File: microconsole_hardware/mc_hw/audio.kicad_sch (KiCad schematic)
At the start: 46 parts, among them U20 PCM5102APWR, U21 PAM8302AADCR, U22 PAM8406DR

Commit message: update
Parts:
- added FB2, FB3: FerriteBead_Small, PCM_SparkFun-Capacitor:C_0603_1608Metric, symbol Device:FerriteBead_Small
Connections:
- net 3v3: now also FB3.1
- net 3v3_AUDIO: now also FB3.2
- net AMP_VDD: now also FB2.2
- new net VBUS: FB2.1

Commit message: charging pass
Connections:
- net VBUS renamed VSYS_BAT

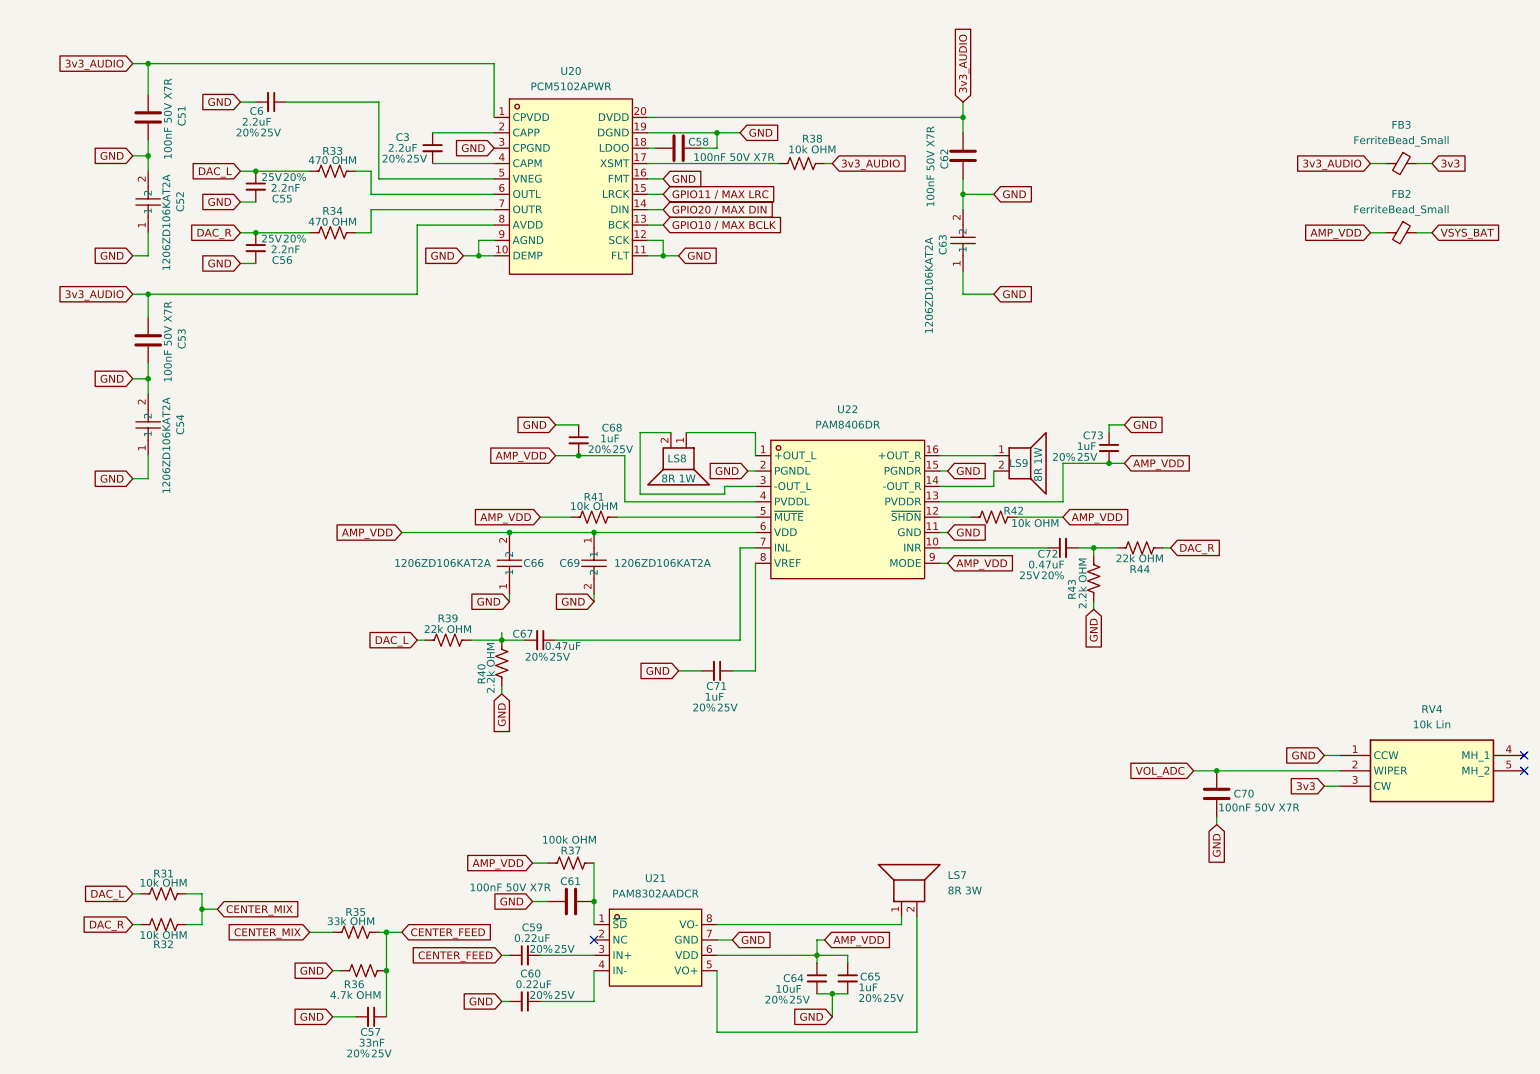
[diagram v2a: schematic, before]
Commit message: recover lost pages
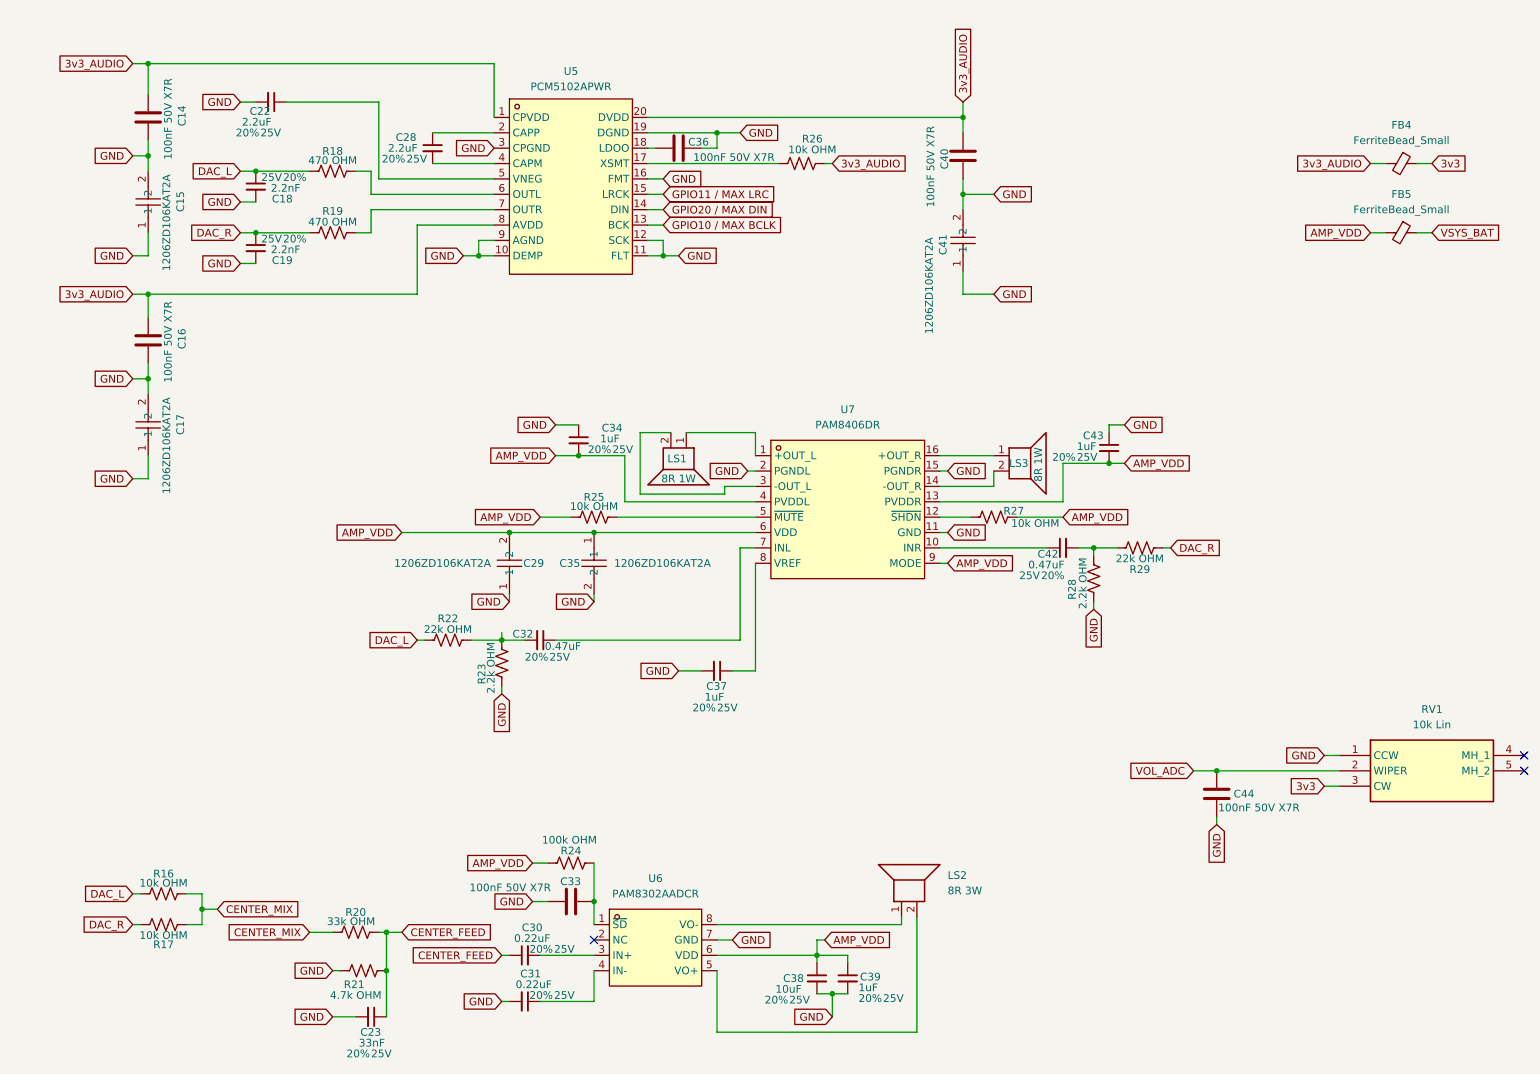
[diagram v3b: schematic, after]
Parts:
- renumbered C51 to C14, C52 to C15, C53 to C16, C54 to C17, C55 to C18, C56 to C19, C6 to C22, C57 to C23, C3 to C28, C66 to C29, C59 to C30, C60 to C31, C67 to C32, C61 to C33, C68 to C34, C69 to C35, C58 to C36, C71 to C37, C64 to C38, C65 to C39, C62 to C40, C63 to C41, C72 to C42, C73 to C43, C70 to C44, FB3 to FB4, FB2 to FB5, LS8 to LS1, LS7 to LS2, LS9 to LS3, R31 to R16, R32 to R17, R33 to R18, R34 to R19, R35 to R20, R36 to R21, R39 to R22, R40 to R23, R37 to R24, R41 to R25, R38 to R26, R42 to R27, R43 to R28, R44 to R29, RV4 to RV1, U20 to U5, U21 to U6, U22 to U7

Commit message: fix a bunch of footprints and routing
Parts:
- FB4, FB5: footprint PCM_SparkFun-Capacitor:C_0603_1608Metric -> Ferrite_THT:LairdTech_28C0236-0JW-10
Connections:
- net 3v3_AUDIO: now also C15.2, C17.2, C41.2
- net GND: no longer C15.2, C17.2, C41.2
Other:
- moved on the sheet: C14, C15, C17, C22, C40, C41

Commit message: fix up
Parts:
- FB4, FB5: footprint Ferrite_THT:LairdTech_28C0236-0JW-10 -> (none)
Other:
- moved on the sheet: LS2

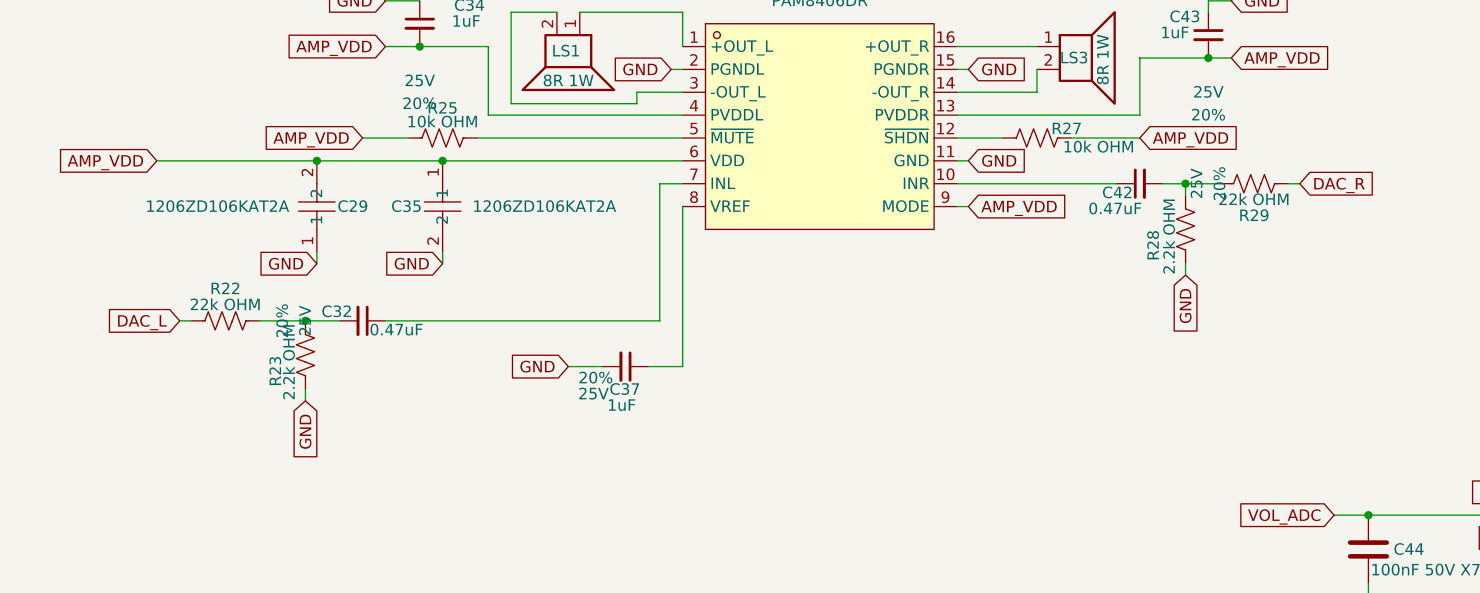
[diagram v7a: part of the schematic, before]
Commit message: fix audio gain, relocated shoulder buttons, round pcb edges
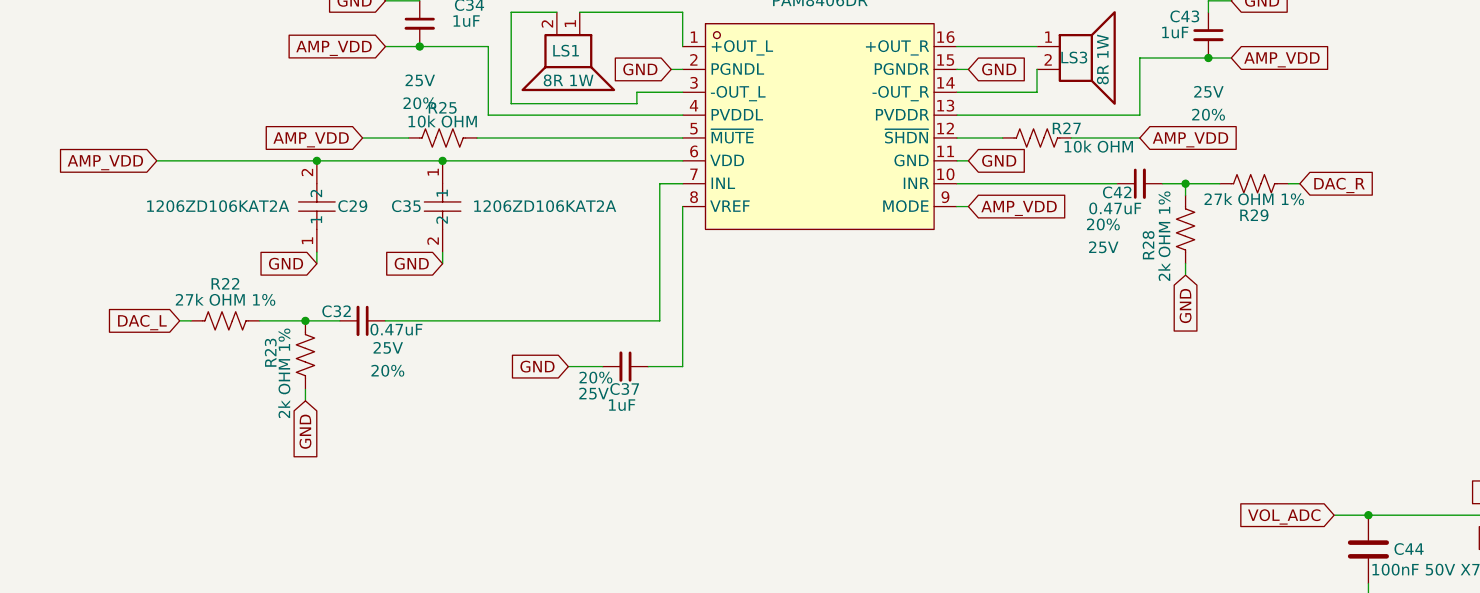
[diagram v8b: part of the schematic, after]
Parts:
- R22, R29: value 22k OHM -> 27k OHM 1%
- R23, R28: value 2.2k OHM -> 2k OHM 1%
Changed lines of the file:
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@@
 		)
 		(property "Voltage" "25V"
-			(at 191.77 107.95 0)
+			(at 181.356 115.062 90)
 			(show_name no)
 			(do_not_autoplace no)
@@
 		)
 		(property "Tolerance" "20%"
-			(at 194.31 107.95 0)
+			(at 181.356 112.522 90)
 			(show_name no)
 			(do_not_autoplace no)
@@
 		(dnp no)
 		(property "Reference" "R28"
-			(at 186.944 114.808 0)
+			(at 186.436 114.808 0)
 			(show_name no)
 			(do_not_autoplace no)
@@
 			)
 		)
-		(property "Value" "2.2k OHM"
-			(at 188.722 113.792 0)
+		(property "Value" "2k OHM 1%"
+			(at 188.214 113.792 0)
 			(show_name no)
 			(do_not_autoplace no)
@@
 		)
 		(property "Voltage" "25V"
-			(at 92.71 123.19 0)
+			(at 101.854 126.238 90)
 			(show_name no)
 			(do_not_autoplace no)
@@
 		)
 		(property "Tolerance" "20%"
-			(at 90.17 123.19 0)
+			(at 101.854 128.778 90)
 			(show_name no)
 			(do_not_autoplace no)
@@
 		(dnp no)
 		(property "Reference" "R22"
-			(at 83.82 119.634 0)
+			(at 83.82 119.126 0)
 			(show_name no)
 			(do_not_autoplace no)
@@
 			)
 		)
-		(property "Value" "22k OHM"
-			(at 83.82 121.412 0)
+		(property "Value" "27k OHM 1%"
+			(at 83.82 120.904 0)
 			(show_name no)
 			(do_not_autoplace no)
@@
 		(dnp no)
 		(property "Reference" "R23"
-			(at 89.408 128.778 0)
+			(at 88.9 126.746 0)
 			(show_name no)
 			(do_not_autoplace no)
@@
 			)
 		)
-		(property "Value" "2.2k OHM"
-			(at 90.932 127.762 0)
+		(property "Value" "2k OHM 1%"
+			(at 90.424 129.032 0)
 			(show_name no)
 			(do_not_autoplace no)
@@
 			)
 		)
-		(property "Value" "22k OHM"
+		(property "Value" "27k OHM 1%"
 			(at 198.12 109.728 0)
 			(show_name no)
